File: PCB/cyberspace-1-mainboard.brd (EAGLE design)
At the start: 180 x 100 mm, 170 parts, among them J10 Header, 8-pin, J11 Header, 8-pin, J12 Header, 8-pin, J13 Header, 8-pin, J14 Header, 8-pin, J15 Header, 8-pin, J16 USB-C, Power, J9 Header, 8-pin, M1 ATmega328P Module, U1 RESET CKT

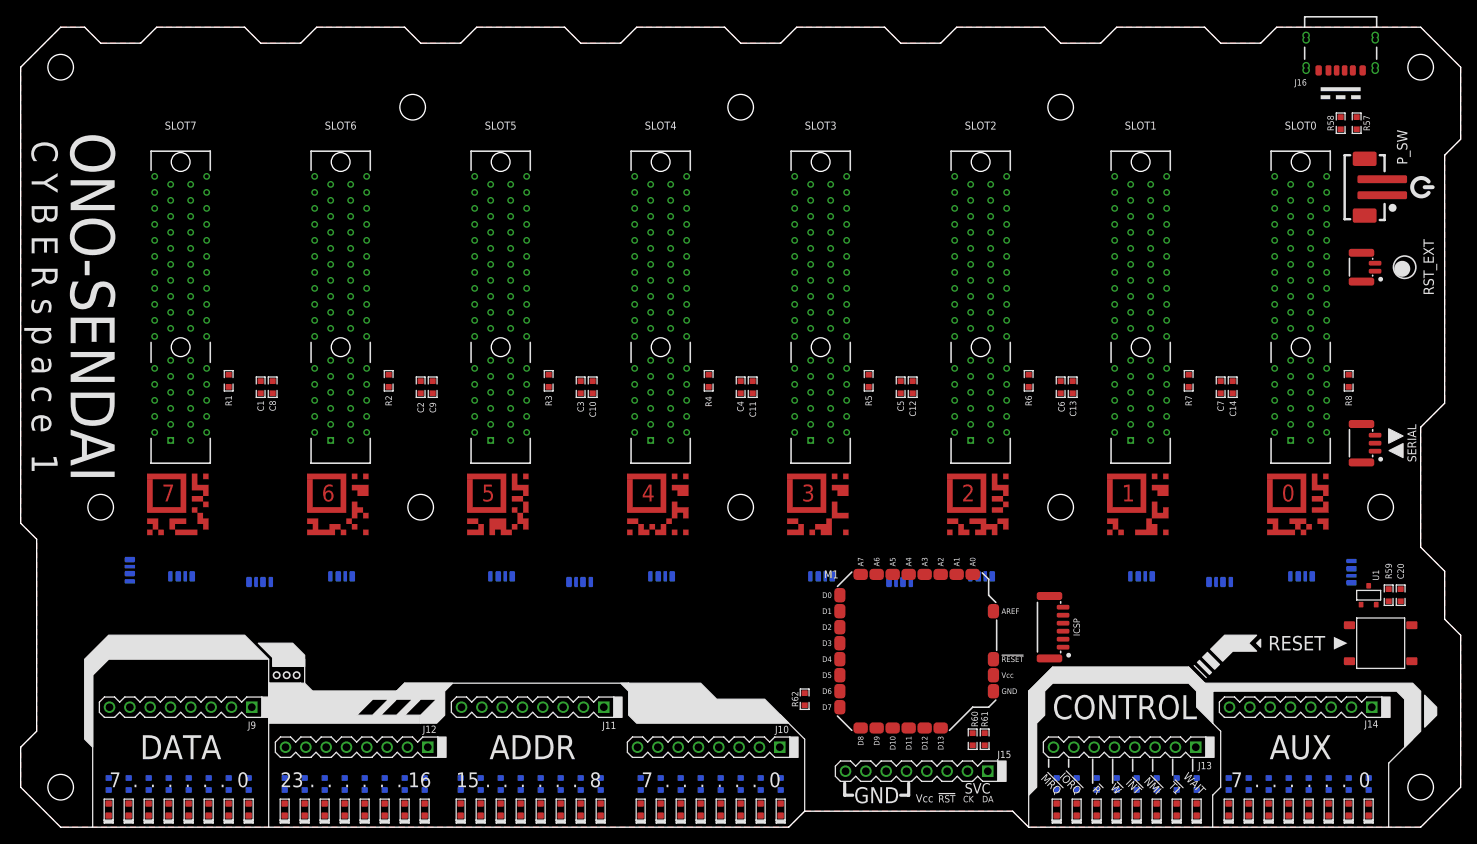
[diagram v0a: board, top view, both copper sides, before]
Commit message: Board routed. Needs tuning.
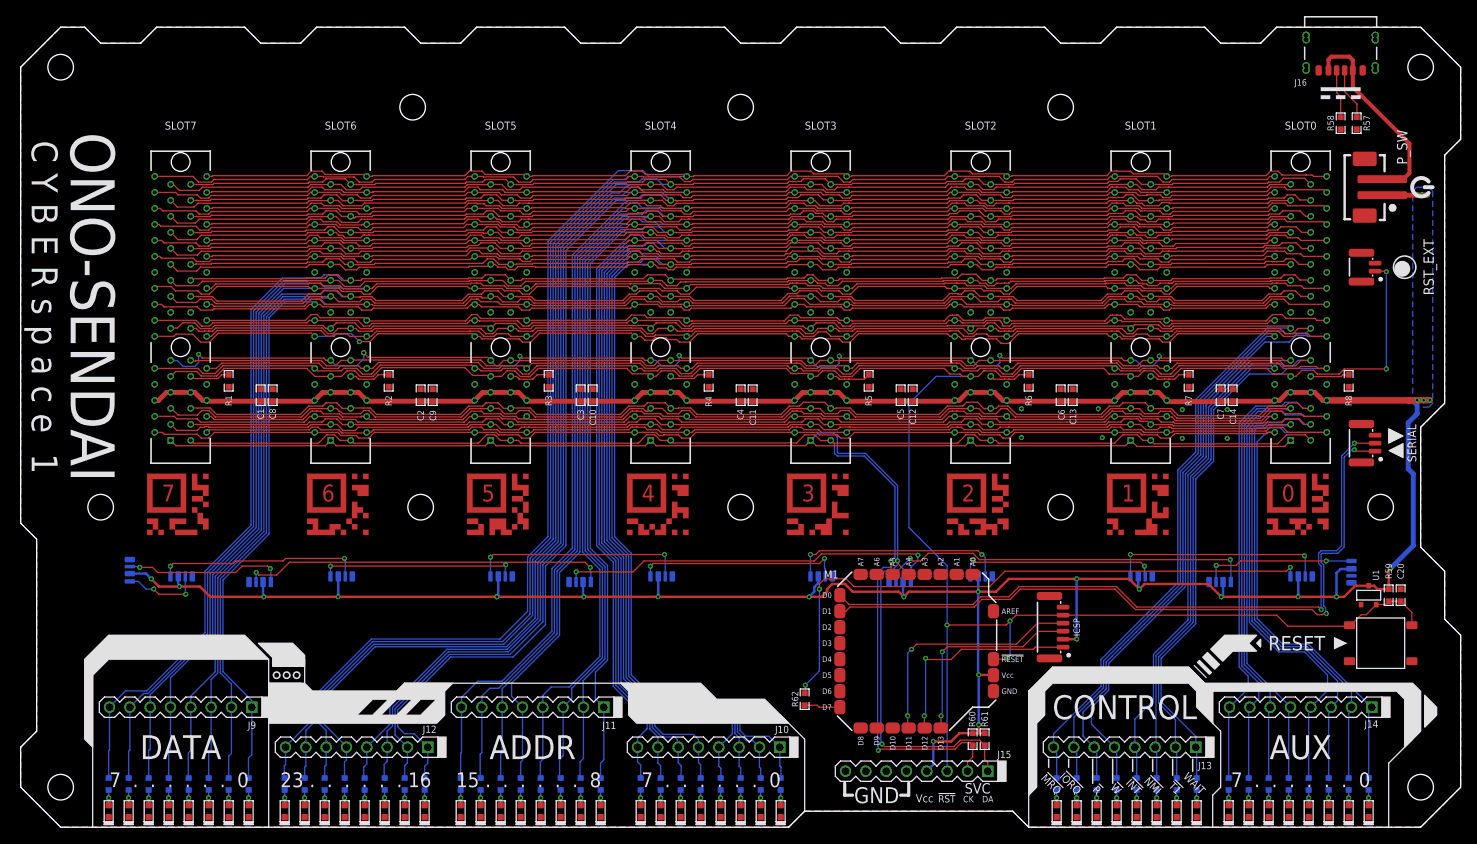
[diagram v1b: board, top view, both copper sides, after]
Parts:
- moved C1 1.00 mm to (30.0, 54.0)
- moved C10 1.00 mm to (71.5, 54.0)
- moved C11 1.00 mm to (91.5, 54.0)
- moved C12 1.00 mm to (111.5, 54.0)
- moved C13 1.00 mm to (131.5, 54.0)
- moved C14 1.00 mm to (151.5, 54.0)
- moved C2 1.00 mm to (50.0, 54.0)
- moved C3 1.00 mm to (70.0, 54.0)
- moved C4 1.00 mm to (90.0, 54.0)
- moved C5 1.00 mm to (110.0, 54.0)
- moved C6 1.00 mm to (130.0, 54.0)
- moved C7 1.00 mm to (150.0, 54.0)
- moved C8 1.00 mm to (31.5, 54.0)
- moved C9 1.00 mm to (51.5, 54.0)
- moved !INT 0.20 mm to (139.5, 2.00)
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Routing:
- net VCC: track 0.00 -> 431.9 mm, vias 0 -> 26
- net !RST: track 0.00 -> 302.5 mm, vias 0 -> 5
- net A23: track 0.00 -> 255.3 mm
- net A21: track 0.00 -> 251.3 mm
- net A20: track 0.00 -> 248.7 mm
- net A22: track 0.00 -> 247.2 mm
- net A19: track 0.00 -> 244.2 mm
- net A17: track 0.00 -> 240.8 mm
- net A16: track 0.00 -> 238.9 mm
- net A18: track 0.00 -> 236.1 mm
- net A15: track 0.00 -> 234.0 mm
- net A3: track 0.00 -> 230.5 mm
- net A11: track 0.00 -> 229.6 mm
- net A1: track 0.00 -> 228.6 mm
- net A13: track 0.00 -> 227.7 mm
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- added copper zone on layer 16, net GND
- added copper zone on layer 16, net VCC

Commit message: Mainboard DRC passed. New stand-in  logo.
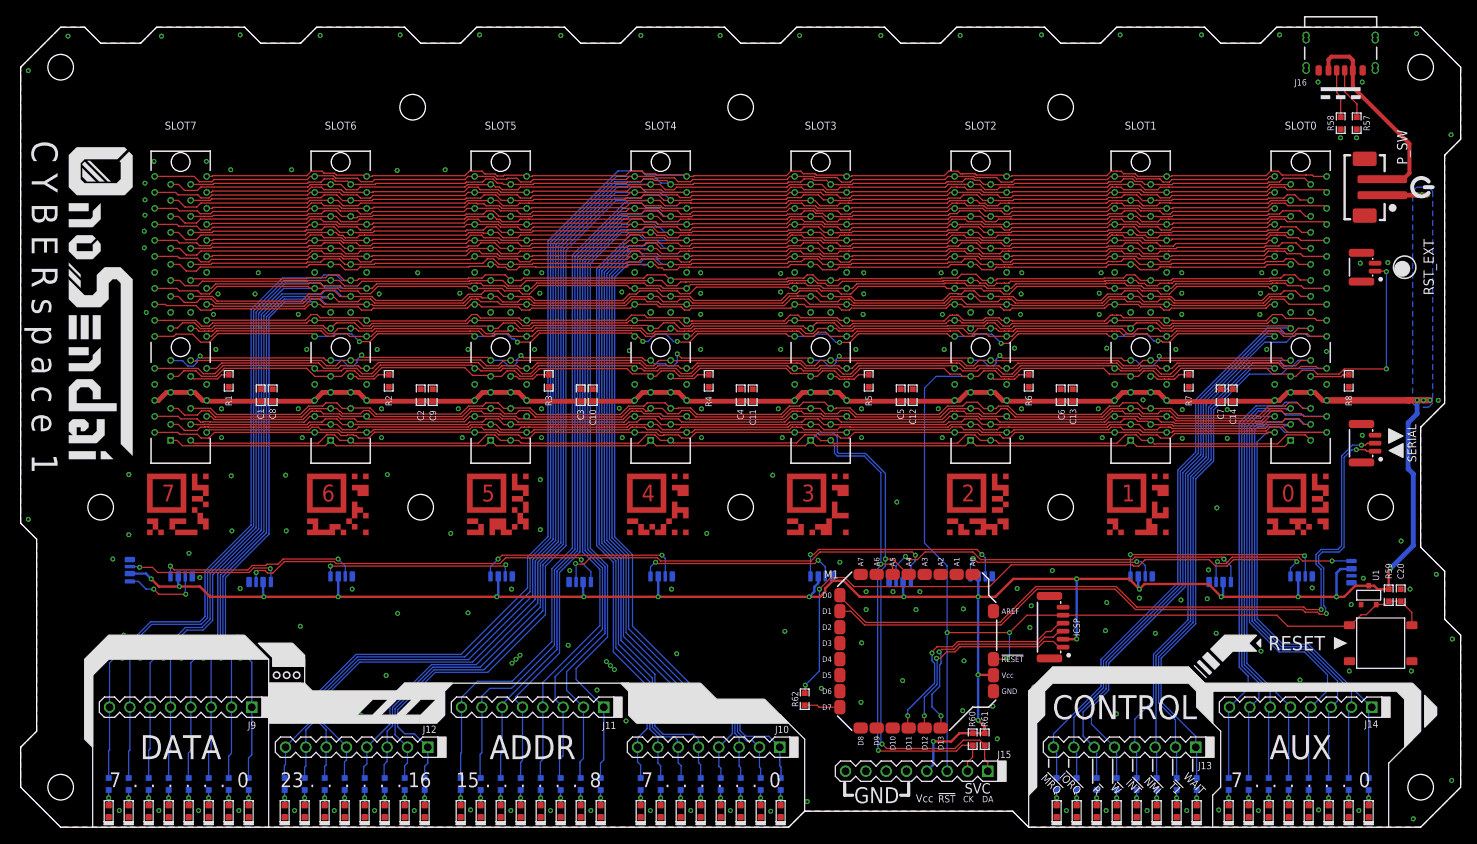
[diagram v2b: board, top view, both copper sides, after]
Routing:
- net A0: track 227.2 -> 223.5 mm
- net A1: track 228.6 -> 225.1 mm
- net A2: track 222.8 -> 219.5 mm
- net D6: track 220.4 -> 223.6 mm
- net A3: track 230.5 -> 227.4 mm
- net N$70: track 76.1 -> 79.0 mm
- net !RST: track 302.5 -> 299.9 mm
- net RX: track 89.3 -> 91.6 mm
- net D7: track 226.1 -> 228.2 mm
- net A8: track 219.8 -> 221.8 mm
- net TX: track 89.8 -> 91.5 mm
- net A9: track 223.3 -> 225.0 mm
- net A23: track 255.3 -> 253.6 mm
- net A11: track 229.6 -> 228.0 mm
- net A22: track 247.2 -> 245.7 mm
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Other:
- board text removed: "ONO-SENDAI"
